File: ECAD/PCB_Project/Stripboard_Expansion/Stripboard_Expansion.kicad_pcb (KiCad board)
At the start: 10 copper layers, 100 x 100.5 mm, 9 parts, among them J1 Inductive, J2 Ultrasonic, J3 Conn_01x03, J4 LDR, J5 LED, J6 MCU, J8 Conn_01x04

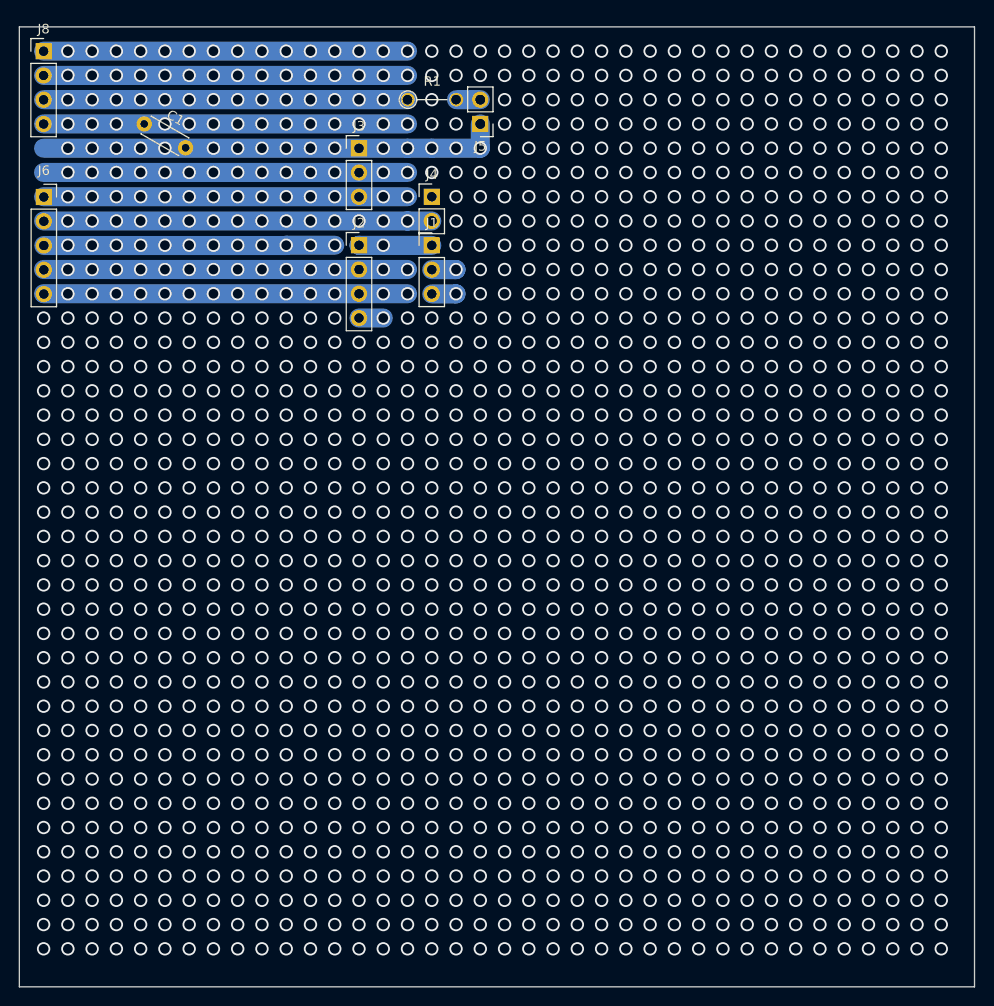
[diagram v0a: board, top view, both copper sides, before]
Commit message: Pushing
COde changes:
MP driver under development
SG90 as well

PCB:
final version, as sent to manufacture

Sims
New sims for report.
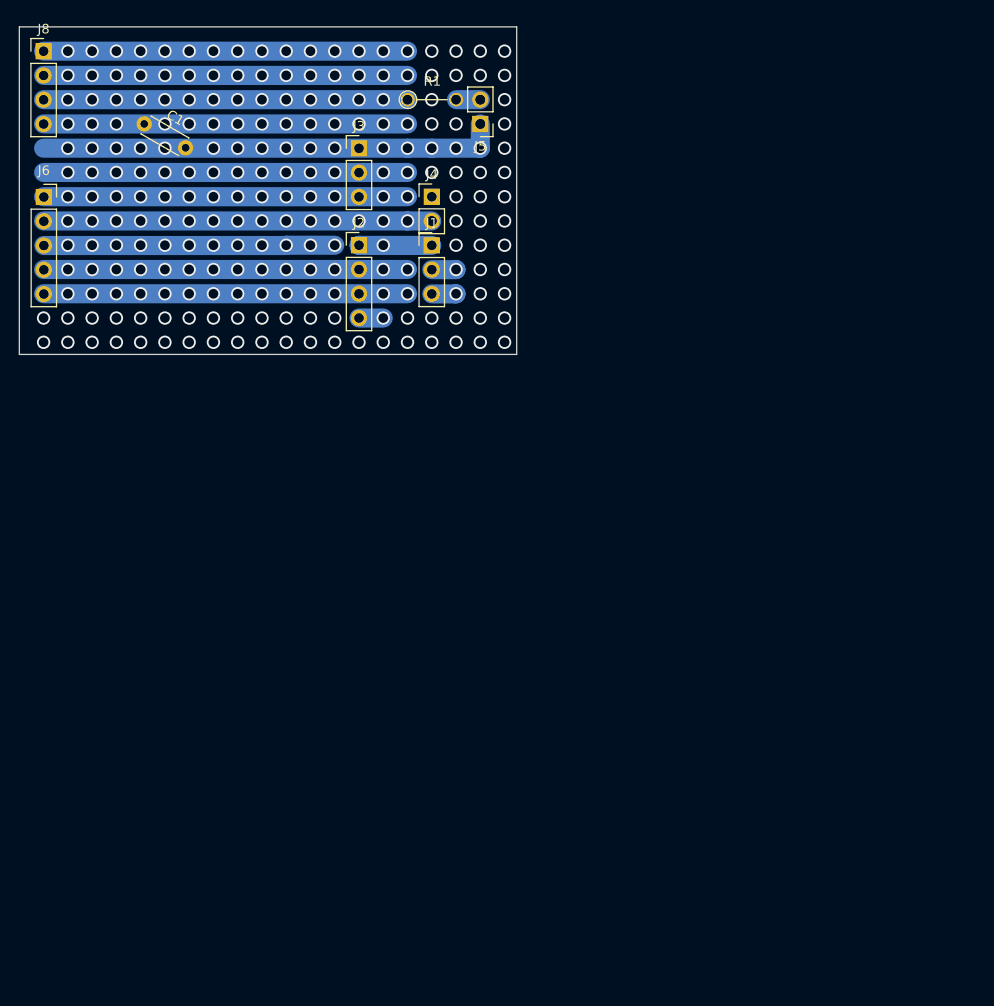
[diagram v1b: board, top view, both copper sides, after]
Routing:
- net (no net): vias 1252 -> 68
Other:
- board size 100 x 100.5 mm -> 52.1 x 34.3 mm
